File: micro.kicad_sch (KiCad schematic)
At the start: 13 parts, among them J3 ST_DBG, U1 STM32F051R8Tx, Y1 Crystal

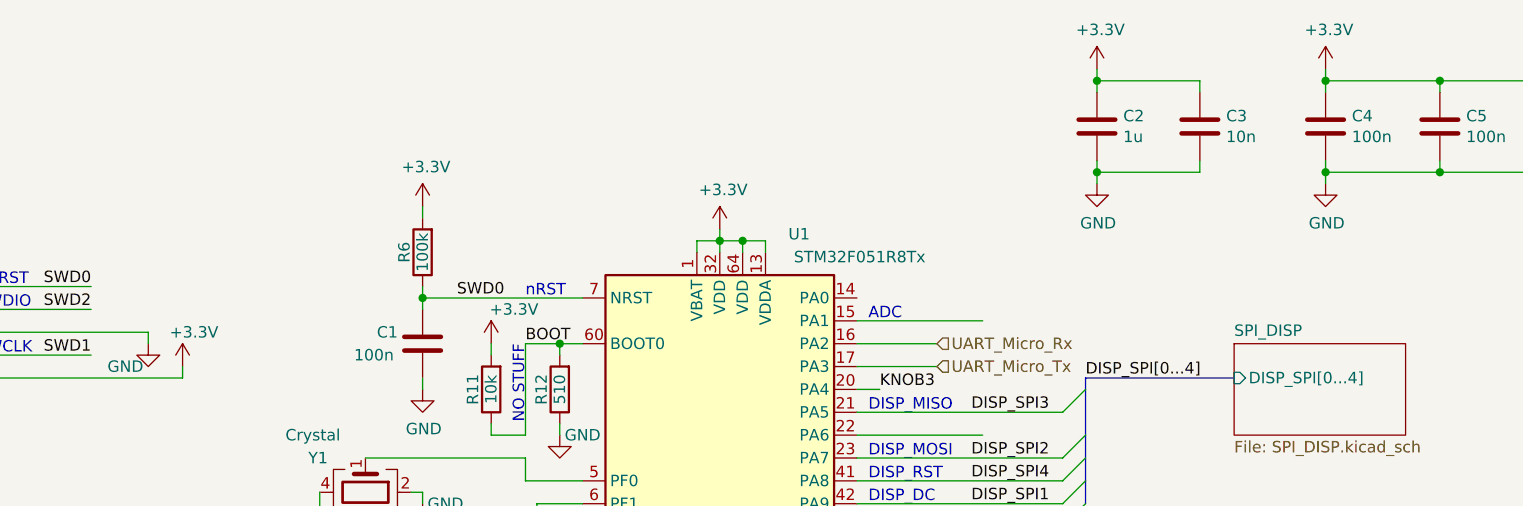
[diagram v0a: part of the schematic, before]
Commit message: update to Kicad v9
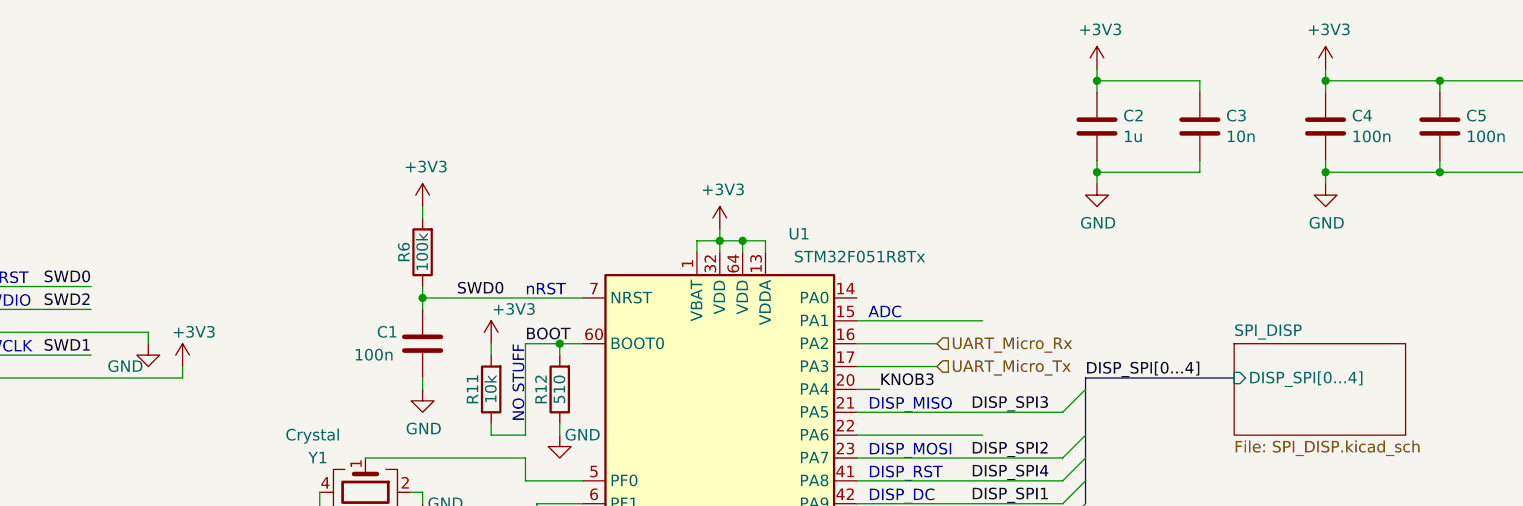
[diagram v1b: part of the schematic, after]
